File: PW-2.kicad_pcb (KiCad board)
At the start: 2 copper layers, 77 parts, among them J1 Conn_01x02_Male, J2 Conn_01x02_Female, J3 USB_A_Stacked, J4 USB_A_Stacked, J5 Conn_02x07_Odd_Even, J6 Conn_01x04_Female, J7 Conn_01x04_Female, Q1 IPT007N06N, Q2 TPH11006NL, Q3 TPH11006NL, SW1 SW_Push, SW2 SW_SPDT, U1 L7812, U2 NCP1034, U3 L78L12_SOT89, U4 MCP1700-3302E_SOT23, U5 STM32F303K8Tx, U6 IM920s, U7 MCP2551-I-SN, Y1 16MHz

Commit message: some
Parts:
- removed J4: USB_A_Stacked, Connector_USB:USB_A_Wuerth_61400826021_Horizontal_Stacked
- added H1: MountingHole, MountingHole:MountingHole_3.2mm_M3_Pad_Via, F.Cu at (143.5, 73.0)
- added H2: MountingHole, MountingHole:MountingHole_3.2mm_M3_Pad_Via, F.Cu at (212.1, 72.4)
- added H3: MountingHole, MountingHole:MountingHole_3.2mm_M3_Pad_Via, F.Cu at (212.1, 157.5)
- added H4: MountingHole, MountingHole:MountingHole_3.2mm_M3_Pad_Via, F.Cu at (143.5, 157.5)
- added J10: Conn_01x02_Male, Connector_PinHeader_2.54mm:PinHeader_1x02_P2.54mm_Vertical, F.Cu at (244.2, 110.2)
- added J11: Conn_01x02_Male, Connector_PinHeader_2.54mm:PinHeader_1x02_P2.54mm_Vertical, F.Cu at (244.2, 86.5)
- added J12: Conn_01x02_Male, Connector_PinHeader_2.54mm:PinHeader_1x02_P2.54mm_Vertical, F.Cu at (244.2, 114.8)
- added J13: Conn_01x02_Male, Connector_PinHeader_2.54mm:PinHeader_1x02_P2.54mm_Vertical, F.Cu at (249.4, 120.0)
- added J14: Conn_01x02_Female, Connector_JST:JST_XA_S02B-XASK-1_1x02_P2.50mm_Horizontal, F.Cu at (150.2, 137.8)
- added J15: Conn_01x02_Female, Connector_JST:JST_XA_S02B-XASK-1_1x02_P2.50mm_Horizontal, F.Cu at (170.2, 150.8)
- added J16: Conn_01x02_Female, Connector_JST:JST_XA_S02B-XASK-1_1x02_P2.50mm_Horizontal, F.Cu at (160.7, 150.8)
- added J17: Conn_01x02_Female, Connector_JST:JST_XA_S02B-XASK-1_1x02_P2.50mm_Horizontal, F.Cu at (151.1, 150.8)
- added J18: Conn_01x02_Female, Connector_JST:JST_XA_S02B-XASK-1_1x02_P2.50mm_Horizontal, F.Cu at (209.8, 99.0)
- added J19: Conn_01x02_Female, Connector_JST:JST_XA_S02B-XASK-1_1x02_P2.50mm_Horizontal, F.Cu at (209.8, 116.8)
- added J20: Conn_01x02_Female, Connector_JST:JST_XA_S02B-XASK-1_1x02_P2.50mm_Horizontal, F.Cu at (209.8, 107.9)
- added J8: Conn_01x02_Female, Connector_T_connector:T_connecter_female_horizontal, F.Cu at (192.4, 73.0)
- added J9: Conn_01x02_Male, Connector_PinHeader_2.54mm:PinHeader_1x02_P2.54mm_Vertical, F.Cu at (249.4, 124.7)
- added JP2: SolderJumper_2_Open, Jumper:SolderJumper-2_P1.3mm_Open_RoundedPad1.0x1.5mm, F.Cu at (243.7, 105.7)
- added JP3: SolderJumper_2_Open, Jumper:SolderJumper-2_P1.3mm_Open_RoundedPad1.0x1.5mm, F.Cu at (250.9, 106.8)
- added JP4: SolderJumper_2_Open, Jumper:SolderJumper-2_P1.3mm_Open_RoundedPad1.0x1.5mm, F.Cu at (247.2, 102.5)
- added JP5: SolderJumper_2_Open, Jumper:SolderJumper-2_P1.3mm_Open_RoundedPad1.0x1.5mm, F.Cu at (250.9, 111.2)
- added JP6: SolderJumper_2_Open, Jumper:SolderJumper-2_P1.3mm_Open_RoundedPad1.0x1.5mm, F.Cu at (250.9, 115.5)
- added R18: 10, Resistor_SMD:R_0603_1608Metric, F.Cu at (253.9, 115.7)
- added R19: 330, Resistor_SMD:R_0603_1608Metric, F.Cu at (253.9, 111.7)
- added SW3: SW_SPDT, Button_Switch_additional:IS-1245T-G, F.Cu at (142.9, 148.6)
- added U8: TLP152, Package_SO_additional:SO-6_5pin_4.4x3.6mm_P1.27mm, F.Cu at (184.8, 99.1)
- moved U3 57.2 mm to (177.2, 98.4), turned to 180 degrees
- moved D5 51.9 mm to (182.9, 158.8), turned to -90 degrees
- moved D4 49.2 mm to (178.4, 158.8), turned to -90 degrees
- moved SW2 36.6 mm to (217.2, 151.8), turned to 90 degrees
- moved C19 31.2 mm to (251.9, 145.8)
- moved C21 31.2 mm to (241.0, 158.7)
- moved C23 31.2 mm to (237.0, 158.7)
- moved R17 31.2 mm to (243.7, 155.7)
- moved SW1 31.2 mm to (242.4, 151.1)
- moved U4 31.2 mm to (252.3, 139.0)
- moved C12 31.2 mm to (239.5, 155.9)
- moved C14 31.2 mm to (246.6, 151.5)
- moved C16 31.2 mm to (250.6, 149.0)
- moved C20 31.2 mm to (256.0, 142.5)
- moved C22 31.2 mm to (246.6, 149.0)
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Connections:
- Q1 pad 1: /main_breaker_gate -> Net-(Q1-Pad1)
- U5 pad 10: /IM920_IO5 -> /IM920_IO4
- U5 pad 11: /IM920_IO3 -> /IM920_IO5
- U5 pad 12: /IM920_IO4 -> /IM920_IO8
- U5 pad 13: /IM920_IO8 -> /IM920_IO10
- U5 pad 14: unconnected-(U5-Pad14) -> /breaker_signal
- U5 pad 18: /IM920_IO10 -> /IM920_RESET
- U5 pad 19: /VCP_RX -> /IM920_IO6
- U5 pad 20: /VCP_TX -> /IM920_IO7
- U5 pad 25: unconnected-(U5-Pad25) -> /VCP_RX
- U5 pad 26: unconnected-(U5-Pad26) -> /disable_remote_kill
- U5 pad 27: unconnected-(U5-Pad27) -> /SW_IN1
- U5 pad 28: unconnected-(U5-Pad28) -> /SW_IN2
- U5 pad 29: unconnected-(U5-Pad29) -> /SW_IN3
- U5 pad 30: unconnected-(U5-Pad30) -> /SW_IN4
- U5 pad 8: /IM920_IO6 -> /VCP_TX
- U5 pad 9: /IM920_IO7 -> /IM920_IO3
- U6 pad 19: unconnected-(U6-Pad19) -> /IM920_RESET

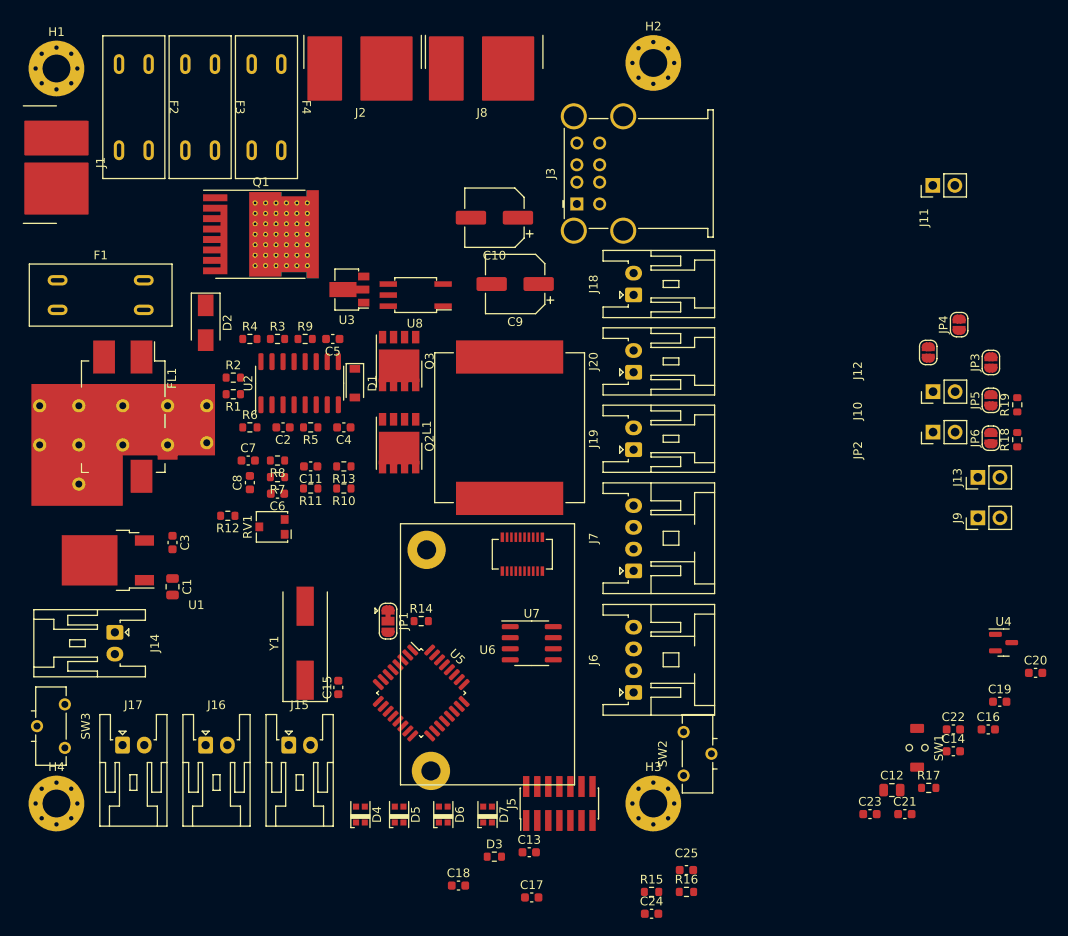
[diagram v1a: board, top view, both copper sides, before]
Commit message: drawing around power done
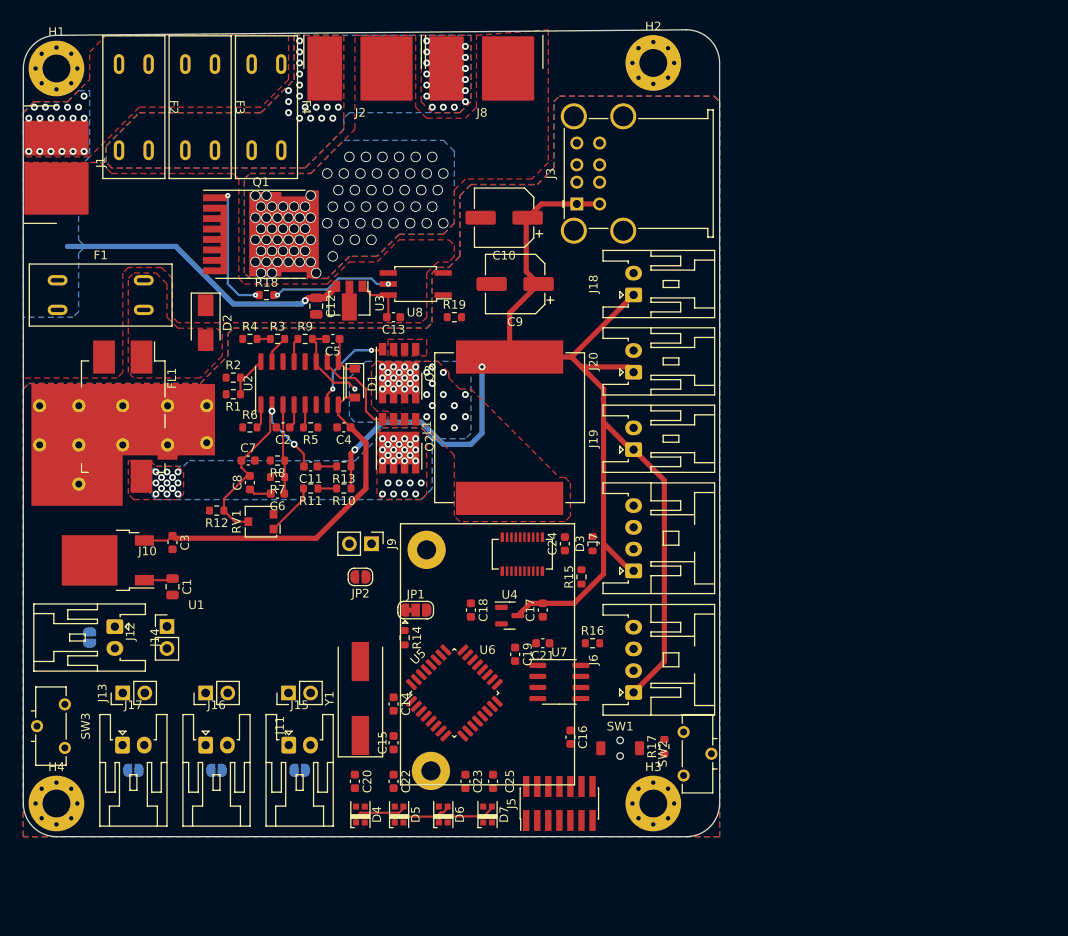
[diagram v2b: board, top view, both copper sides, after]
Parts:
- JP3, JP4, JP5, JP6: moved to B.Cu
- Q1: footprint Package_TO_SOT_SMD:Infineon_PG-HSOF-8-1_ThermalVias -> Package_TO_SOT_SMD:Infineon_PG-HSOF-8-1
- moved JP3 108.3 mm to (147.3, 138.4), turned to -90 degrees
- moved JP6 105.7 mm to (152.3, 153.7), turned to 0 degrees
- moved J13 101.3 mm to (151.1, 144.8)
- moved JP5 98.6 mm to (161.9, 153.7), turned to 0 degrees
- moved J11 94.2 mm to (170.2, 144.8)
- moved J10 92.1 mm to (156.2, 137.1), turned to 0 degrees
- moved JP4 91.5 mm to (171.4, 153.7), turned to 0 degrees
- moved J12 88.8 mm to (160.7, 144.8)
- moved R18 87.9 mm to (167.6, 99.1), turned to 0 degrees
- moved C12 86.4 mm to (173.4, 100.3), turned to -90 degrees
- moved C20 79.2 mm to (177.8, 154.9), turned to -90 degrees
- moved JP2 70.2 mm to (178.4, 131.4), turned to 180 degrees
- moved J9 69.7 mm to (179.7, 127.6), turned to -90 degrees
- moved R19 65.5 mm to (189.2, 101.6), turned to 0 degrees
- moved C22 64.6 mm to (182.2, 154.9), turned to -90 degrees
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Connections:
- J6 pad 1: unconnected-(J6-Pad1) -> +5V
- J6 pad 4: unconnected-(J6-Pad4) -> GND
- J7 pad 1: unconnected-(J7-Pad1) -> +5V
- J7 pad 4: unconnected-(J7-Pad4) -> GND
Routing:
- net +5V: track 0.00 -> 158.8 mm, vias 0 -> 2
- net Net-(C3-Pad1): track 0.00 -> 41.3 mm
- net +BATT: track 0.00 -> 34.5 mm, vias 0 -> 19
- net Net-(C11-Pad2): track 0.00 -> 25.9 mm, vias 0 -> 2
- net Net-(Q1-Pad1): track 0.00 -> 15.8 mm, vias 0 -> 2
- net /main_breaker_gate: track 0.00 -> 14.2 mm, vias 0 -> 2
- net Net-(Q2-Pad4): track 0.00 -> 10.8 mm
- net Net-(Q3-Pad4): track 0.00 -> 10.8 mm, vias 0 -> 2
- net Net-(C5-Pad2): track 0.00 -> 10.3 mm, vias 0 -> 32
- net Net-(C6-Pad1): track 0.00 -> 10.3 mm
- net Net-(D5-Pad1): track 0.00 -> 7.29 mm
- net Net-(D6-Pad1): track 0.00 -> 7.14 mm
- net Net-(D4-Pad1): track 0.00 -> 6.68 mm
- net Net-(R11-Pad2): track 0.00 -> 6.08 mm
- net +12P: track 0.00 -> 6.00 mm
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- added copper zone on B.Cu, net +BATT
- added copper zone on F.Cu, net +BATT
- added copper zone on B.Cu, net /5V_supply/24V_supply
- added copper zone on F.Cu, net /5V_supply/24V_supply
- added copper zone on B.Cu, net /Vout+
- added copper zone on F.Cu, net /Vout+
- added copper zone on B.Cu, net /Vout-
- added copper zone on F.Cu, net /Vout-
- added copper zone on B.Cu, net GND
- added copper zone on F.Cu, net GND
- added copper zone on F.Cu, net GNDPWR
- added copper zone on B.Cu, net Net-(C5-Pad2)
- added copper zone on F.Cu, net Net-(C5-Pad2)
- added copper zone on F.Cu, net Net-(D2-Pad2)
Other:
- board outline added: 80 x 92.7 mm

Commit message: v0 done!
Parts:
- moved C19 1.55 mm to (196.2, 141.9), turned to 90 degrees
- moved C16 1.27 mm to (202.6, 151.1)
- moved U4 1.08 mm to (196.3, 135.1)
- moved J3 0.20 mm to (203.3, 88.4)
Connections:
- SW2 pad 1: /CANH -> unconnected-(SW2-Pad1)
- SW2 pad 3: unconnected-(SW2-Pad3) -> /CANH
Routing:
- net +3V3: track 0.00 -> 65.2 mm, vias 0 -> 8
- net /breaker_signal: track 0.00 -> 60.7 mm, vias 0 -> 2
- net /SW_IN1: track 0.00 -> 55.2 mm, vias 0 -> 1
- net +5V: track 158.8 -> 212.3 mm, vias 2 -> 6
- net /SW_IN4: track 0.00 -> 47.5 mm, vias 0 -> 1
- net /VCP_RX: track 0.00 -> 37.3 mm, vias 0 -> 2
- net /SW_IN3: track 0.00 -> 37.3 mm, vias 0 -> 1
- net /CANL: track 0.00 -> 36.4 mm
- net /CANH: track 0.00 -> 32.3 mm
- net /IM920_IO3: track 0.00 -> 31.5 mm, vias 0 -> 2
- net /IM920_IO5: track 0.00 -> 30.9 mm, vias 0 -> 2
- net /IM920_IO1: track 0.00 -> 30.0 mm, vias 0 -> 2
- net /NRST: track 0.00 -> 29.9 mm
- net /SW_IN2: track 0.00 -> 29.3 mm, vias 0 -> 1
- net /IM920_IO2: track 0.00 -> 27.4 mm, vias 0 -> 2
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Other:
- board text added: "BOOT0 0⇔1"
- board text added: "Batt In"
- board text added: "C7 10n C9, C10 100u C6, C8, C11 1n C1, C12 10u C2, C3, C5, C13, C16, C19-C25 100n C14, C15 22p C4, C17, C18 1u D1 D D2 D_TVS D3 LED D4-D7 WS2812C F1-F4 Fuse FL1 BNX022 J1 T_conn_male J3 USB_A_Stacked J5 2x07_P1.27mm_SMD J6, J7 S04B-XASK-1 J2, J8 T_conn_female J9-J13 PinHeader_1x02_P2.54mm J14-J20 S02B-XASK-1 JP1 SolderJumper_3_Bridged12 JP2-JP6 SolderJumper_2_Open L1 8.2uH Q1 IPT007N06N Q2, Q3 TP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"
- board text added: "Designed by paripal https://github.com/paripalpp/PW-2"
- board text added: "EM SW PB5-7"
- board text added: "EN ↕ DS"
- board text added: "Main SW PB4"
- board text added: "Main off⇔on"
- board text added: "PW-2_v0"
- board text added: "Power Out"
- board text added: "Power supply board"
- board text added: "R term"
- board text added: "RST"
